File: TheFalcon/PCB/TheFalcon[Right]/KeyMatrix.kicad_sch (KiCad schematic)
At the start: 76 parts

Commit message: save
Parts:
- D10: renamed from D9; footprint (none) -> Diode_SMD:D_SOD-123
- D11: renamed from D10; footprint (none) -> Diode_SMD:D_SOD-123
- D12: renamed from D11; footprint (none) -> Diode_SMD:D_SOD-123
- D13: renamed from D12; footprint (none) -> Diode_SMD:D_SOD-123
- D14: renamed from D13; footprint (none) -> Diode_SMD:D_SOD-123
- D15: renamed from D14; footprint (none) -> Diode_SMD:D_SOD-123
- D16: renamed from D15; footprint (none) -> Diode_SMD:D_SOD-123
- D17: renamed from D16; footprint (none) -> Diode_SMD:D_SOD-123
- D18: renamed from D17; footprint (none) -> Diode_SMD:D_SOD-123
- D19: renamed from D18; footprint (none) -> Diode_SMD:D_SOD-123
- D2: renamed from D1; footprint (none) -> Diode_SMD:Nexperia_CFP3_SOD-123W
- D20: renamed from D19; footprint (none) -> Diode_SMD:D_SOD-123
- D21: renamed from D20; footprint (none) -> Diode_SMD:D_SOD-123
- D22: renamed from D21; footprint (none) -> Diode_SMD:D_SOD-123
- D23: renamed from D22; footprint (none) -> Diode_SMD:D_SOD-123
- D24: renamed from D23; footprint (none) -> Diode_SMD:D_SOD-123
- D25: renamed from D24; footprint (none) -> Diode_SMD:D_SOD-123
- D26: renamed from D25; footprint (none) -> Diode_SMD:D_SOD-123
- D27: renamed from D26; footprint (none) -> Diode_SMD:D_SOD-123
- D28: renamed from D27; footprint (none) -> Diode_SMD:D_SOD-123
- D29: renamed from D28; footprint (none) -> Diode_SMD:D_SOD-123
- D3: renamed from D2; footprint (none) -> Diode_SMD:D_SOD-123
- D30: renamed from D29; footprint (none) -> Diode_SMD:D_SOD-123
- D31: renamed from D30; footprint (none) -> Diode_SMD:D_SOD-123
- D32: renamed from D31; footprint (none) -> Diode_SMD:D_SOD-123
- D33: renamed from D32; footprint (none) -> Diode_SMD:D_SOD-123
- D34: renamed from D33; footprint (none) -> Diode_SMD:D_SOD-123
- D35: renamed from D34; footprint (none) -> Diode_SMD:D_SOD-123
- D36: renamed from D35; footprint (none) -> Diode_SMD:D_SOD-123
- D37: renamed from D36; footprint (none) -> Diode_SMD:D_SOD-123
- D38: renamed from D37; footprint (none) -> Diode_SMD:D_SOD-123
- D39: renamed from D38; footprint (none) -> Diode_SMD:D_SOD-123
- D4: renamed from D3; footprint (none) -> Diode_SMD:D_SOD-123
- D5: renamed from D4; footprint (none) -> Diode_SMD:D_SOD-123
- D6: renamed from D5; footprint (none) -> Diode_SMD:D_SOD-123
- D7: renamed from D6; footprint (none) -> Diode_SMD:D_SOD-123
- D8: renamed from D7; footprint (none) -> Diode_SMD:D_SOD-123
- D9: renamed from D8; footprint (none) -> Diode_SMD:D_SOD-123
- S26: footprint Gateron_KS33_Hotswap:Gateron-KS33-Hotswap-1.5U -> Gateron_KS33_Hotswap:Gateron-KS33-Hotswap-1U
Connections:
- net at D39.2 (A): now also S38.2
- net at D27.2 (A): now also S26.2
- net at S32.2: now also D33.2 (A)
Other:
- title: (none) -> TheFalcon[Left[

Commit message: Save
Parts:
- removed D32, D38: Diode, Diode_SMD:D_SOD-123, symbol ScottoKeebs:Placeholder_Diode
- removed S31, S37: Keyswitch, Gateron_KS33_Hotswap:Gateron-KS33-Hotswap-1U, symbol ScottoKeebs:Placeholder_Keyswitch
- S1, S18: footprint Gateron_KS33_Hotswap:Gateron-KS33-Hotswap-1U -> MX_KS33:MX_KS33-Solderable-1U
- S10: renamed from S12; footprint Gateron_KS33_Hotswap:Gateron-KS33-Hotswap-1U -> MX_KS33:MX_KS33-Solderable-1U
- S11: renamed from S17; footprint Gateron_KS33_Hotswap:Gateron-KS33-Hotswap-1U -> MX_KS33:MX_KS33-Solderable-1U
- S12: renamed from S22; footprint Gateron_KS33_Hotswap:Gateron-KS33-Hotswap-1U -> MX_KS33:MX_KS33-Solderable-1U
- S13: renamed from S28; footprint Gateron_KS33_Hotswap:Gateron-KS33-Hotswap-1U -> MX_KS33:MX_KS33-Solderable-1U
- S14: renamed from S34; footprint Gateron_KS33_Hotswap:Gateron-KS33-Hotswap-1U -> MX_KS33:MX_KS33-Solderable-1U
- S15: renamed from S3; footprint Gateron_KS33_Hotswap:Gateron-KS33-Hotswap-1U -> MX_KS33:MX_KS33-Solderable-1U
- S16: renamed from S8; footprint Gateron_KS33_Hotswap:Gateron-KS33-Hotswap-1U -> MX_KS33:MX_KS33-Solderable-1U
- S17: renamed from S13; footprint Gateron_KS33_Hotswap:Gateron-KS33-Hotswap-1U -> MX_KS33:MX_KS33-Solderable-1U
- S19: renamed from S23; footprint Gateron_KS33_Hotswap:Gateron-KS33-Hotswap-1U -> MX_KS33:MX_KS33-Solderable-1U
- S2: renamed from S6; footprint Gateron_KS33_Hotswap:Gateron-KS33-Hotswap-1U -> MX_KS33:MX_KS33-Solderable-1U
- S20: renamed from S29; footprint Gateron_KS33_Hotswap:Gateron-KS33-Hotswap-1U -> MX_KS33:MX_KS33-Solderable-1U
- S21: renamed from S35; footprint Gateron_KS33_Hotswap:Gateron-KS33-Hotswap-1U -> MX_KS33:MX_KS33-Solderable-1U
- S22: renamed from S4; footprint Gateron_KS33_Hotswap:Gateron-KS33-Hotswap-1U -> MX_KS33:MX_KS33-Solderable-1U
- S23: renamed from S9; footprint Gateron_KS33_Hotswap:Gateron-KS33-Hotswap-1U -> MX_KS33:MX_KS33-Solderable-1U
- S24: renamed from S14; footprint Gateron_KS33_Hotswap:Gateron-KS33-Hotswap-1U -> MX_KS33:MX_KS33-Solderable-1U
- S25: renamed from S19; footprint Gateron_KS33_Hotswap:Gateron-KS33-Hotswap-1U -> MX_KS33:MX_KS33-Solderable-1U
- S26: renamed from S24; footprint Gateron_KS33_Hotswap:Gateron-KS33-Hotswap-1U -> MX_KS33:MX_KS33-Solderable-1U
- S27: renamed from S30; footprint Gateron_KS33_Hotswap:Gateron-KS33-Hotswap-1U -> MX_KS33:MX_KS33-Solderable-1U
- S28: renamed from S36; footprint Gateron_KS33_Hotswap:Gateron-KS33-Hotswap-1U -> MX_KS33:MX_KS33-Solderable-1U
- S29: renamed from S5; footprint Gateron_KS33_Hotswap:Gateron-KS33-Hotswap-1U -> MX_KS33:MX_KS33-Solderable-1U
- S3: renamed from S11; footprint Gateron_KS33_Hotswap:Gateron-KS33-Hotswap-1U -> MX_KS33:MX_KS33-Solderable-1U
- S30: renamed from S10; footprint Gateron_KS33_Hotswap:Gateron-KS33-Hotswap-1U -> MX_KS33:MX_KS33-Solderable-1U
- S31: renamed from S15; footprint Gateron_KS33_Hotswap:Gateron-KS33-Hotswap-1U -> MX_KS33:MX_KS33-Solderable-1U
- S32: renamed from S20; footprint Gateron_KS33_Hotswap:Gateron-KS33-Hotswap-1U -> MX_KS33:MX_KS33-Solderable-1U
- S33: renamed from S25; footprint Gateron_KS33_Hotswap:Gateron-KS33-Hotswap-1U -> MX_KS33:MX_KS33-Solderable-1U
- S34: renamed from S26; footprint Gateron_KS33_Hotswap:Gateron-KS33-Hotswap-1U -> MX_KS33:MX_KS33-Solderable-1U
- S35: renamed from S32; footprint Gateron_KS33_Hotswap:Gateron-KS33-Hotswap-1.5U -> MX_KS33:MX_KS33-Solderable-1.5U
- S36: renamed from S38; footprint Gateron_KS33_Hotswap:Gateron-KS33-Hotswap-1.5U -> MX_KS33:MX_KS33-Solderable-1.5U
- S4: renamed from S16; footprint Gateron_KS33_Hotswap:Gateron-KS33-Hotswap-1U -> MX_KS33:MX_KS33-Solderable-1U
- S5: renamed from S21; footprint Gateron_KS33_Hotswap:Gateron-KS33-Hotswap-1U -> MX_KS33:MX_KS33-Solderable-1U
- S6: renamed from S27; footprint Gateron_KS33_Hotswap:Gateron-KS33-Hotswap-1U -> MX_KS33:MX_KS33-Solderable-1U
- S7: renamed from S33; footprint Gateron_KS33_Hotswap:Gateron-KS33-Hotswap-1U -> MX_KS33:MX_KS33-Solderable-1U
- S8: renamed from S2; footprint Gateron_KS33_Hotswap:Gateron-KS33-Hotswap-1U -> MX_KS33:MX_KS33-Solderable-1U
- S9: renamed from S7; footprint Gateron_KS33_Hotswap:Gateron-KS33-Hotswap-1U -> MX_KS33:MX_KS33-Solderable-1U
- renumbered D13 to D10, D18 to D11, D23 to D12, D29 to D13, D35 to D14, D4 to D15, D9 to D16, D14 to D17, D19 to D18, D24 to D19, D7 to D2, D30 to D20, D36 to D21, D5 to D22, D10 to D23, D15 to D24, D20 to D25, D25 to D26, D31 to D27, D37 to D28, D6 to D29, D12 to D3, D11 to D30, D16 to D31, D21 to D32, D26 to D33, D27 to D36, D33 to D37, D39 to D38, D17 to D4, D22 to D5, D28 to D6, D34 to D7, D3 to D8, D8 to D9
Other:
- moved on the sheet: D10, D11, D12, D13, D14, D15, D16, D17, D18, D19, D2, D20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

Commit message: Save
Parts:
- renumbered D2 to D1, D36 to D34, D37 to D35, D38 to D36
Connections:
- net Col0: now also S14.1, S21.1, S28.1, S36.1, S7.1; no longer S1.1, S15.1, S22.1, S29.1, S8.1
- net Col1: now also S13.1, S20.1, S27.1, S35.1, S6.1; no longer S16.1, S2.1, S23.1, S30.1, S9.1
- net Col2: now also S12.1, S19.1, S26.1, S33.1, S34.1, S5.1; no longer S10.1, S17.1, S24.1, S3.1, S31.1
- net Col4: now also S10.1, S17.1, S24.1, S3.1, S31.1; no longer S12.1, S19.1, S26.1, S33.1, S34.1, S5.1
- net Col5: now also S16.1, S2.1, S23.1, S30.1, S9.1; no longer S13.1, S20.1, S27.1, S35.1, S6.1
- net Col6: now also S1.1, S15.1, S22.1, S29.1, S8.1; no longer S14.1, S21.1, S28.1, S36.1, S7.1
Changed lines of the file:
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@@
 	(global_label "Col5"
 		(shape input)
-		(at 91.44 27.94 90)
+		(at 40.64 27.94 90)
 		(fields_autoplaced yes)
 		(effects
@@
 		)
 		(property "Intersheetrefs" "${INTERSHEET_REFS}"
-			(at 91.44 20.6611 90)
+			(at 40.64 20.6611 90)
 			(effects
 				(font
@@
 	(global_label "Col4"
 		(shape input)
-		(at 78.74 27.94 90)
+		(at 53.34 27.94 90)
 		(fields_autoplaced yes)
 		(effects
@@
 		)
 		(property "Intersheetrefs" "${INTERSHEET_REFS}"
-			(at 78.74 20.6611 90)
+			(at 53.34 20.6611 90)
 			(effects
 				(font
@@
 	(global_label "Col0"
 		(shape input)
-		(at 27.94 27.94 90)
+		(at 104.14 27.94 90)
 		(fields_autoplaced yes)
 		(effects
@@
 		)
 		(property "Intersheetrefs" "${INTERSHEET_REFS}"
-			(at 27.94 20.6611 90)
+			(at 104.14 20.6611 90)
 			(effects
 				(font
@@
 	(global_label "Col1"
 		(shape input)
-		(at 40.64 27.94 90)
+		(at 91.44 27.94 90)
 		(fields_autoplaced yes)
 		(effects
@@
 		)
 		(property "Intersheetrefs" "${INTERSHEET_REFS}"
-			(at 40.64 20.6611 90)
+			(at 91.44 20.6611 90)
 			(effects
 				(font
@@
 	(global_label "Col6"
 		(shape input)
-		(at 104.14 27.94 90)
+		(at 27.94 27.94 90)
 		(fields_autoplaced yes)
 		(effects
@@
 		)
 		(property "Intersheetrefs" "${INTERSHEET_REFS}"
-			(at 104.14 20.6611 90)
+			(at 27.94 20.6611 90)
 			(effects
 				(font
@@
 	(global_label "Col2"
 		(shape input)
-		(at 53.34 27.94 90)
+		(at 78.74 27.94 90)
 		(fields_autoplaced yes)
 		(effects
@@
 		)
 		(property "Intersheetrefs" "${INTERSHEET_REFS}"
-			(at 53.34 20.6611 90)
+			(at 78.74 20.6611 90)
 			(effects
 				(font
@@
 		(dnp no)
 		(fields_autoplaced yes)
-		(property "Reference" "D38"
+		(property "Reference" "D36"
 			(at 111.76 176.5299 90)
 			(effects
@@
 			(project "TheFalcon[Right]"
 				(path "/c04da171-1d33-4593-80a3-c384d6d19f7c/a2a6b3bd-c82e-469c-bf12-2c3386a797ce"
-					(reference "D38")
+					(reference "D36")
 					(unit 1)
 				)
@@
 		(dnp no)
 		(fields_autoplaced yes)
-		(property "Reference" "D36"
+		(property "Reference" "D34"
 			(at 86.36 176.5299 90)
 			(effects
@@
 			(project "TheFalcon[Right]"
 				(path "/c04da171-1d33-4593-80a3-c384d6d19f7c/a2a6b3bd-c82e-469c-bf12-2c3386a797ce"
-					(reference "D36")
+					(reference "D34")
 					(unit 1)
 				)
@@
 		(dnp no)
 		(fields_autoplaced yes)
-		(property "Reference" "D37"
+		(property "Reference" "D35"
 			(at 99.06 176.5299 90)
 			(effects
@@
 			(project "TheFalcon[Right]"
 				(path "/c04da171-1d33-4593-80a3-c384d6d19f7c/a2a6b3bd-c82e-469c-bf12-2c3386a797ce"
-					(reference "D37")
+					(reference "D35")
 					(unit 1)
 				)
@@
 		(dnp no)
 		(fields_autoplaced yes)
-		(property "Reference" "D2"
+		(property "Reference" "D1"
 			(at 35.56 49.5299 90)
 			(effects
@@
 			(project "TheFalcon[Right]"
 				(path "/c04da171-1d33-4593-80a3-c384d6d19f7c/a2a6b3bd-c82e-469c-bf12-2c3386a797ce"
-					(reference "D2")
+					(reference "D1")
 					(unit 1)
 				)

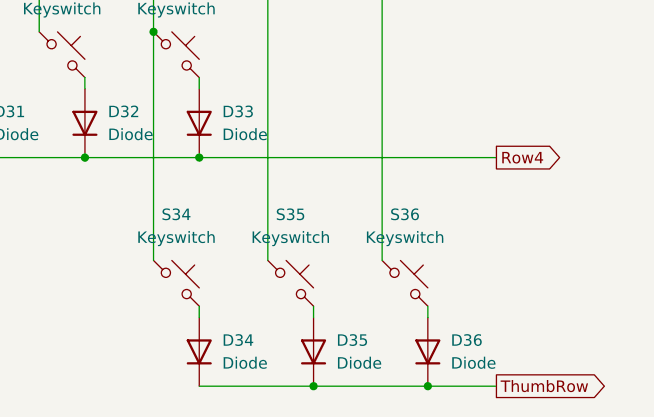
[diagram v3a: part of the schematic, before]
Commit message: Save
Checked right PCB and hole to track spacing for left. Will do check for left pcb tomorrow
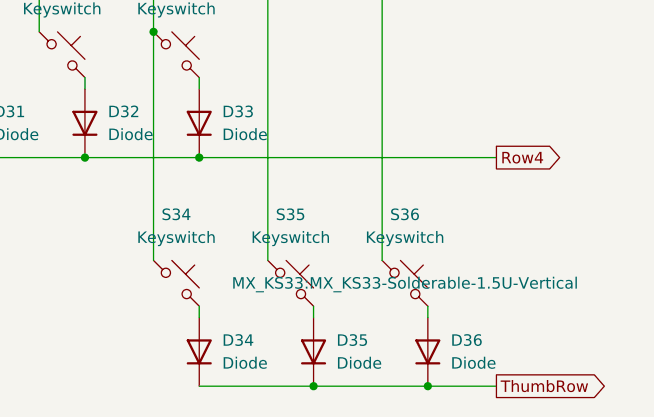
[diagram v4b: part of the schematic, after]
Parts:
- S35, S36: footprint MX_KS33:MX_KS33-Solderable-1.5U -> MX_KS33:MX_KS33-Solderable-1.5U-Vertical
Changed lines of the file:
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@@
 			)
 		)
-		(property "Footprint" "MX_KS33:MX_KS33-Solderable-1.5U"
+		(property "Footprint" "MX_KS33:MX_KS33-Solderable-1.5U-Vertical"
 			(at 93.98 170.18 0)
 			(effects
@@
 			)
 		)
-		(property "Footprint" "MX_KS33:MX_KS33-Solderable-1.5U"
+		(property "Footprint" "MX_KS33:MX_KS33-Solderable-1.5U-Vertical"
 			(at 106.68 170.18 0)
 			(effects
@@
 					(size 1.27 1.27)
 				)
-				(hide yes)
-			)
-		)
+			)
+		)

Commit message: Files ready for production
Going to panelise seperate files to reduce PCBA cost
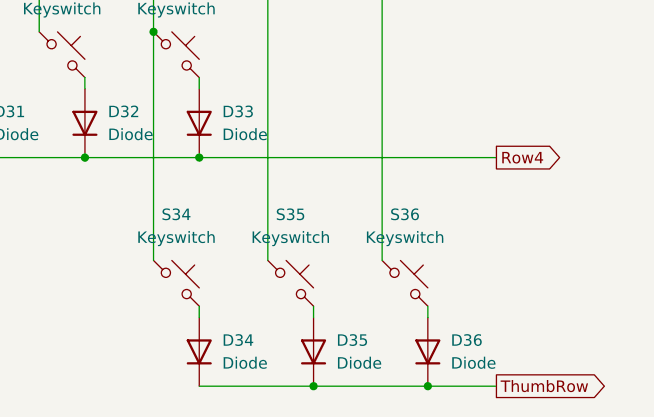
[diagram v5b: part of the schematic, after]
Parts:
- D1: footprint Diode_SMD:Nexperia_CFP3_SOD-123W -> Diode_SMD:D_SOD-123; LCSC Part Number (none) -> C2099
- D10, D11, D12, D13, D14, D15, D16, D17, D18, D19, D2, D20, D21, D22, D23, D24, D25, D26, D27, D28, D29, D3, D30, D31, D32, D33, D34, D35, D36, D4, D5, D6, D7, D8, D9: LCSC Part Number (none) -> C2099
